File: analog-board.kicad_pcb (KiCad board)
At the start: 2 copper layers, 200 x 150 mm, 495 parts, among them J1 AC IN, J2 OUT, J3 CONN_20X2, P2 CONN_01X02, Q1 2N3906, Q10 2N3906, Q11 2N3906, Q12 2N3906, Q13 2N3906, Q14 2N3906, Q15 2N3906, Q16 2N3906, Q17 NPN, Q18 NPN, Q19 J111, Q2 2N3906, Q20 2N3906, Q3 2N3906, Q4 2N3906, Q5 2N3906, Q6 BCM857BS, Q7 2N3906, Q8 2N3906, Q9 2N3906, U1 LM13700, U10 ADR01, U11 DG212B, U12 DG212B, U13 DG408, U14 DG408, U15 TL072-, U16 DG408, U17 DG408, U18 LM13700, U19 LM13700, U2 LM13700, U20 74HC75, U21 TL072-, U22 TL074-, U23 TL074-, U24 TL074-, U25 TL074-, U26 TL072-, U27 TL074-, U28 TL074-, U29 LM13700, U3 LM13700, U30 LM13700, U31 TL074-, U32 LM13700, U33 TL074-, U34 TL074-, U35 TL074-, U36 74LV573, U38 0 - 10V, U39 TL074-, U4 DG212B, U40 DG419, U41 0 - 10V, U42 10 - 0V, U43 LM7812, U44 LM7912, U45 DG408, U46 7805, U5 TL074-, U6 AD5556, U7 TL072-, U8 TL074-, U9 AD8672

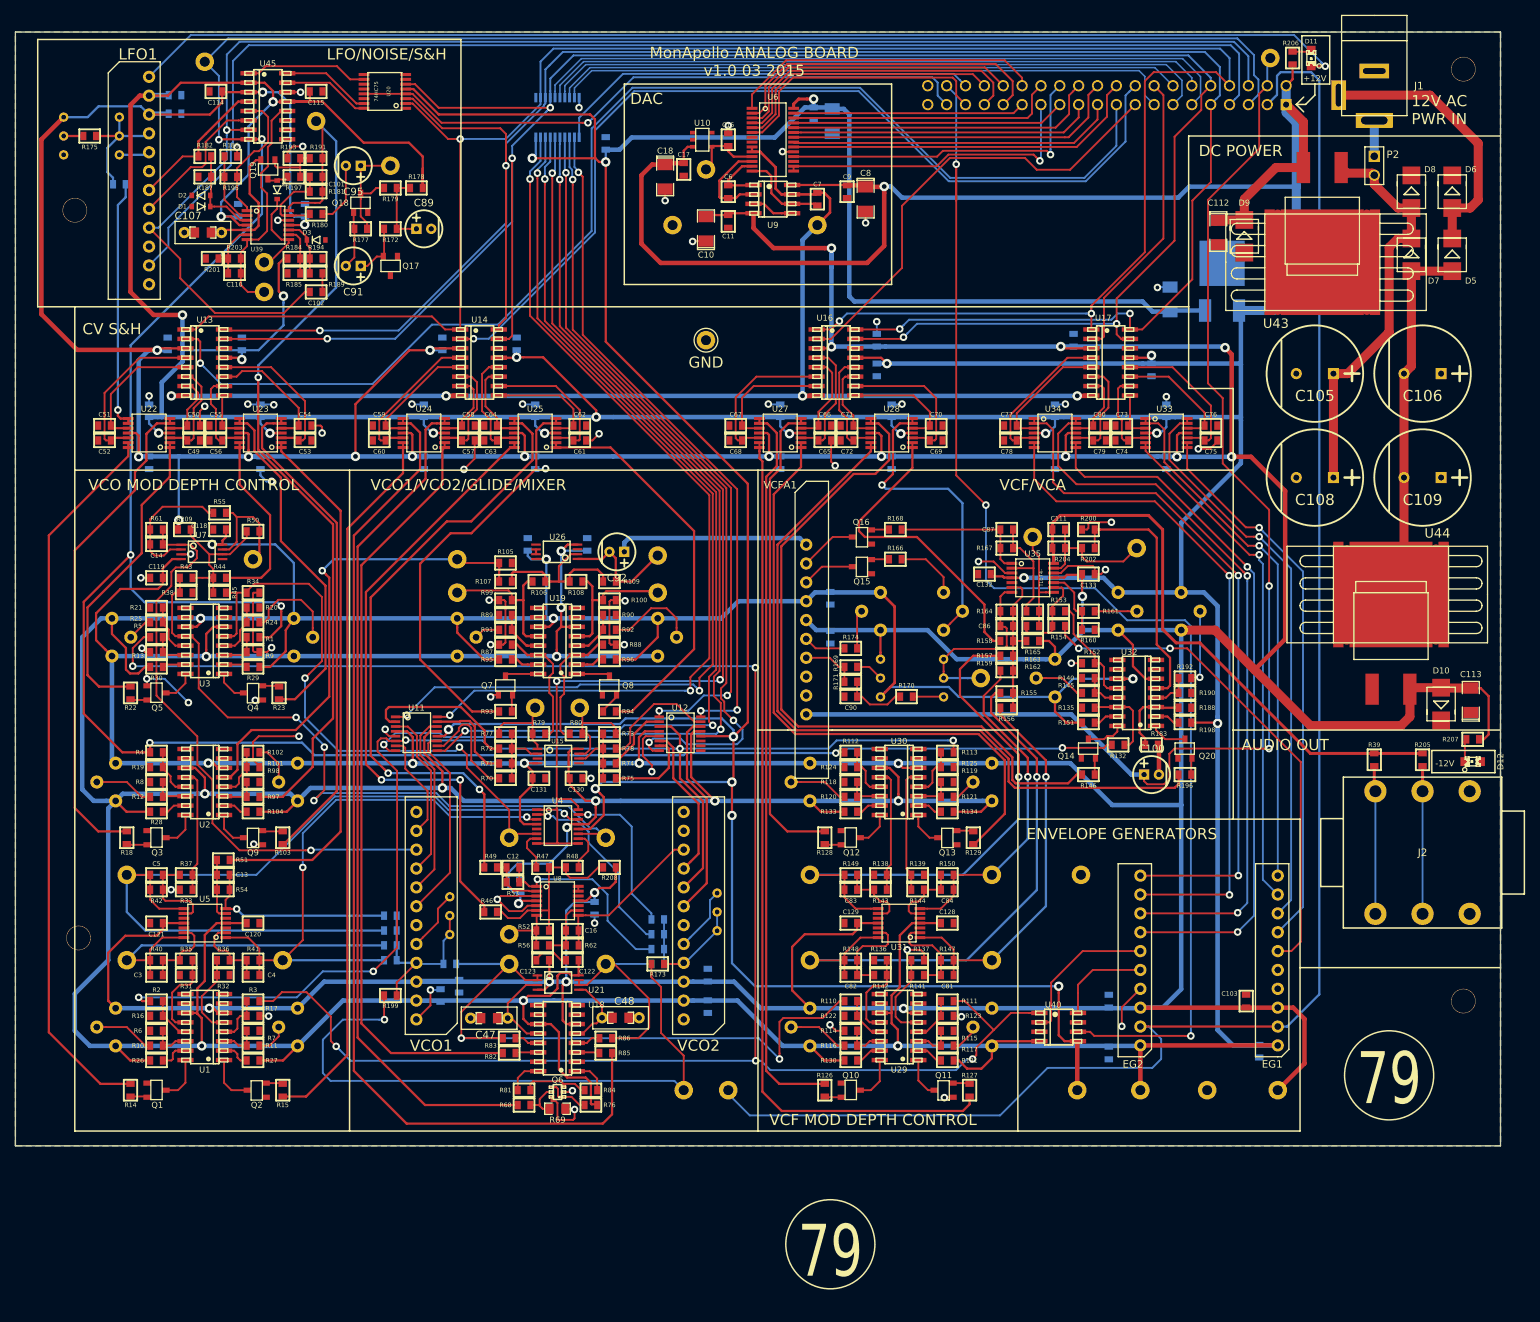
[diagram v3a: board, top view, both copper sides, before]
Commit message: added resistor dividers for pulse output on VCOs and LFO to get 10Vpp pulse level
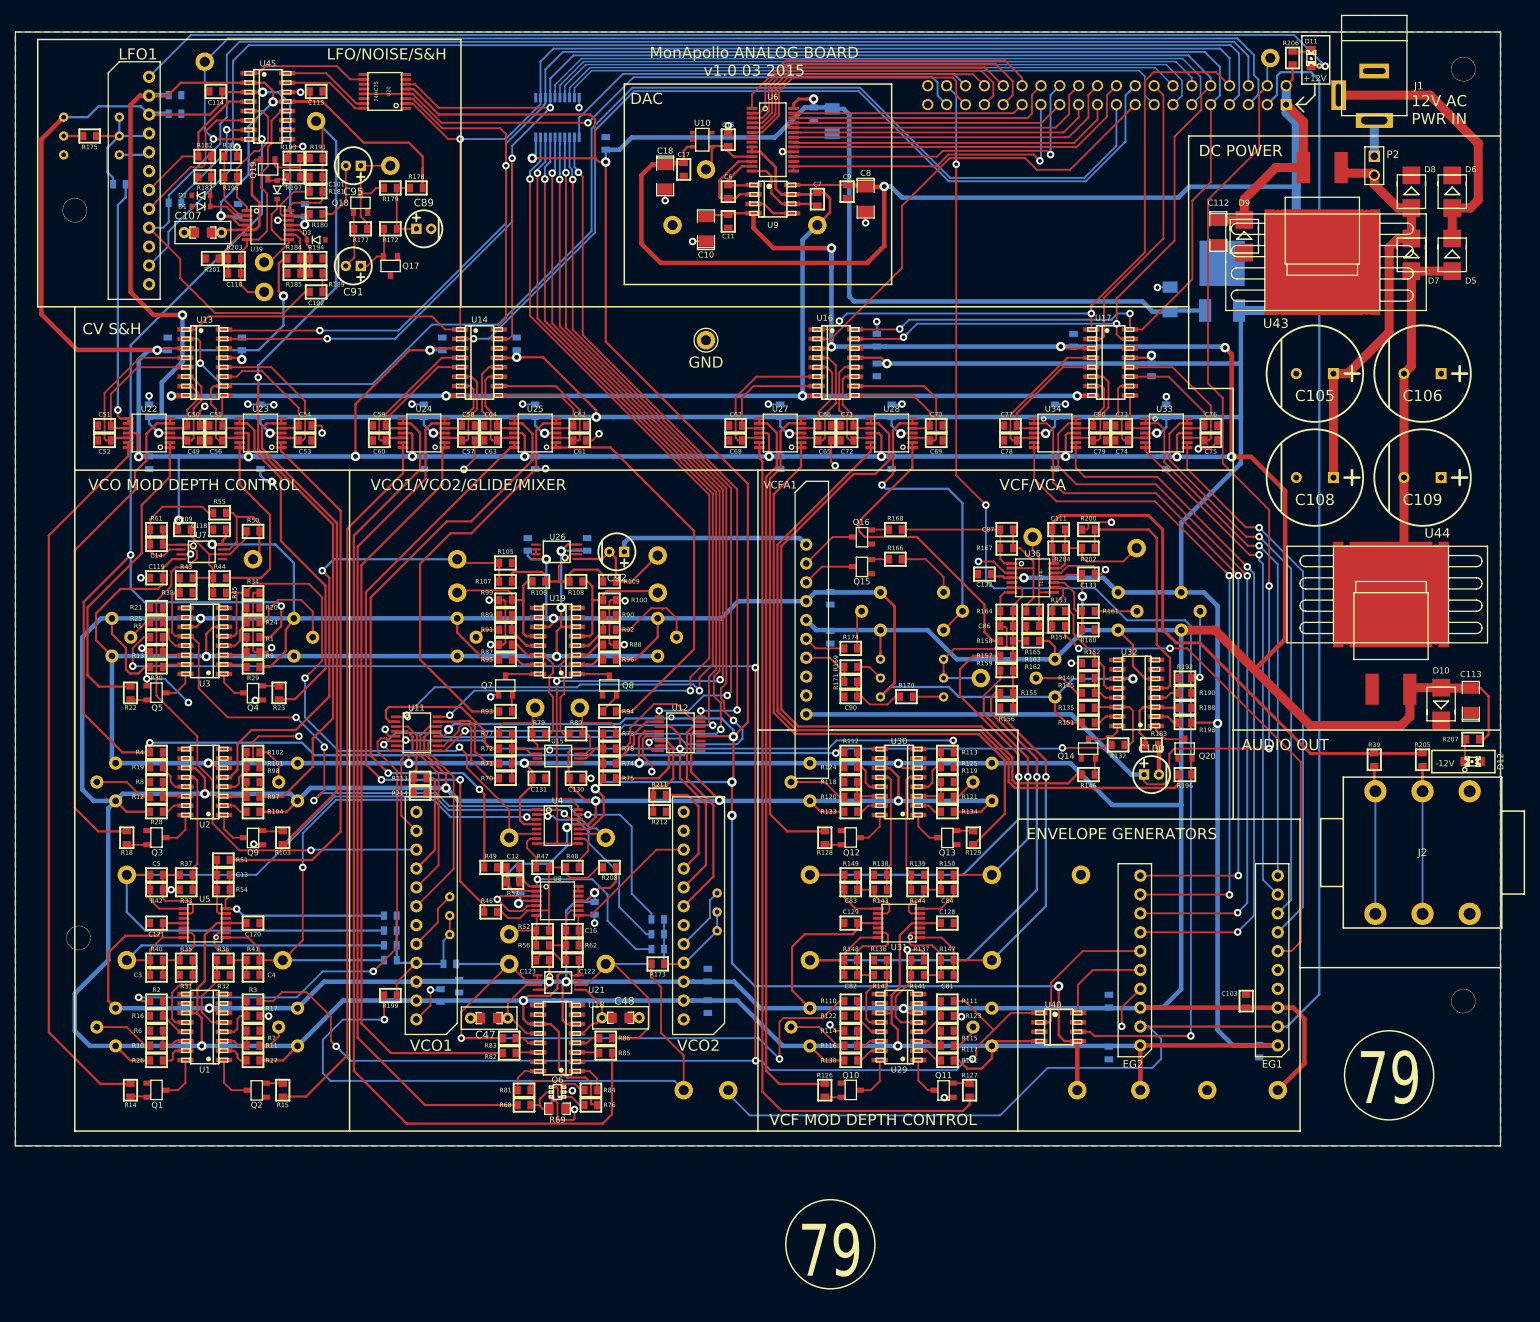
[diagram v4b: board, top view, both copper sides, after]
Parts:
- added R210: 3.3K, MyModules:SM0603-R-JRL, B.Cu at (21.5, 23.0)
- added R211: 10K, MyModules:SM0603-R-JRL, F.Cu at (86.8, 102.8)
- added R212: 9.1K, MyModules:SM0603-R-JRL, F.Cu at (86.8, 105.0)
- added R213: 10K, MyModules:SM0603-R-JRL, F.Cu at (54.5, 100.5)
- added R214: 9.1K, MyModules:SM0603-R-JRL, F.Cu at (54.5, 102.5)
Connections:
- U11 pad 3: Net-(U11-Pad3) -> Net-(R213-Pad1)
- U12 pad 6: Net-(U12-Pad6) -> Net-(R211-Pad1)
- U45 pad 7: LFO TUNE -> Net-(R210-Pad1)
- VCO1 pad 9: Net-(U11-Pad3) -> Net-(R213-Pad2)
- VCO2 pad 9: Net-(U12-Pad6) -> Net-(R211-Pad2)
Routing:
- net Net-(U11-Pad3): track 22.9 -> 0.00 mm
- net Net-(U12-Pad6): track 20.8 -> 0.00 mm
- net Net-(R210-Pad1): track 0.00 -> 15.3 mm, vias 0 -> 1
- net Net-(R211-Pad2): track 0.00 -> 14.2 mm
- net Net-(R213-Pad2): track 0.00 -> 14.2 mm
- net Net-(R211-Pad1): track 0.00 -> 12.8 mm
- net Net-(R213-Pad1): track 0.00 -> 11.3 mm
- net LFO TUNE: track 203.5 -> 201.1 mm, vias 1 -> 0
- net Net-(U11-Pad7): track 14.4 -> 13.3 mm
- net Net-(LFO1-Pad8): track 20.0 -> 20.9 mm
- net Net-(U12-Pad14): track 28.0 -> 28.7 mm
- net Net-(LFO1-Pad7): track 19.5 -> 20.2 mm

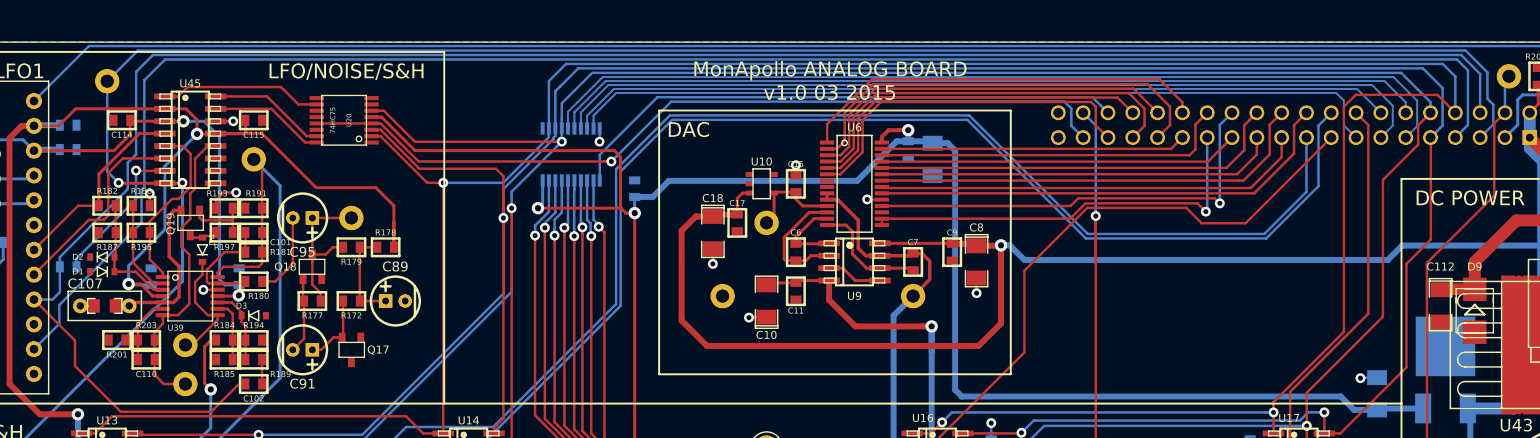
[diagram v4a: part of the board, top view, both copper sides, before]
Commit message: LFO TUNE now connected to S&H clock through R215
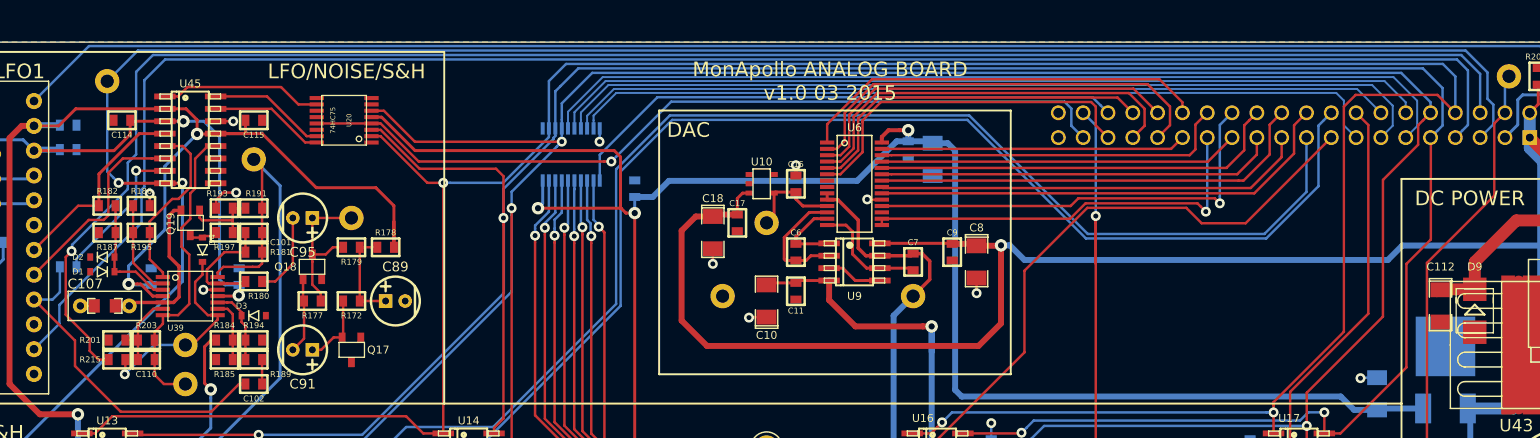
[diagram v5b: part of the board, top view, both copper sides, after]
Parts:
- added R215: 10K, synth:SM0603-JRL, F.Cu at (26.5, 32.5)
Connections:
- C102 pad 1: LFO TUNE -> Net-(C102-Pad1)
- LFO1 pad 9: LFO TUNE -> Net-(C102-Pad1)
- R210 pad 2: LFO TUNE -> Net-(C102-Pad1)
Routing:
- net Net-(C102-Pad1): track 0.00 -> 34.8 mm
- net LFO TUNE: track 201.1 -> 178.1 mm, vias 0 -> 1
- net Net-(D4-Pad2): track 12.1 -> 21.1 mm, vias 0 -> 1

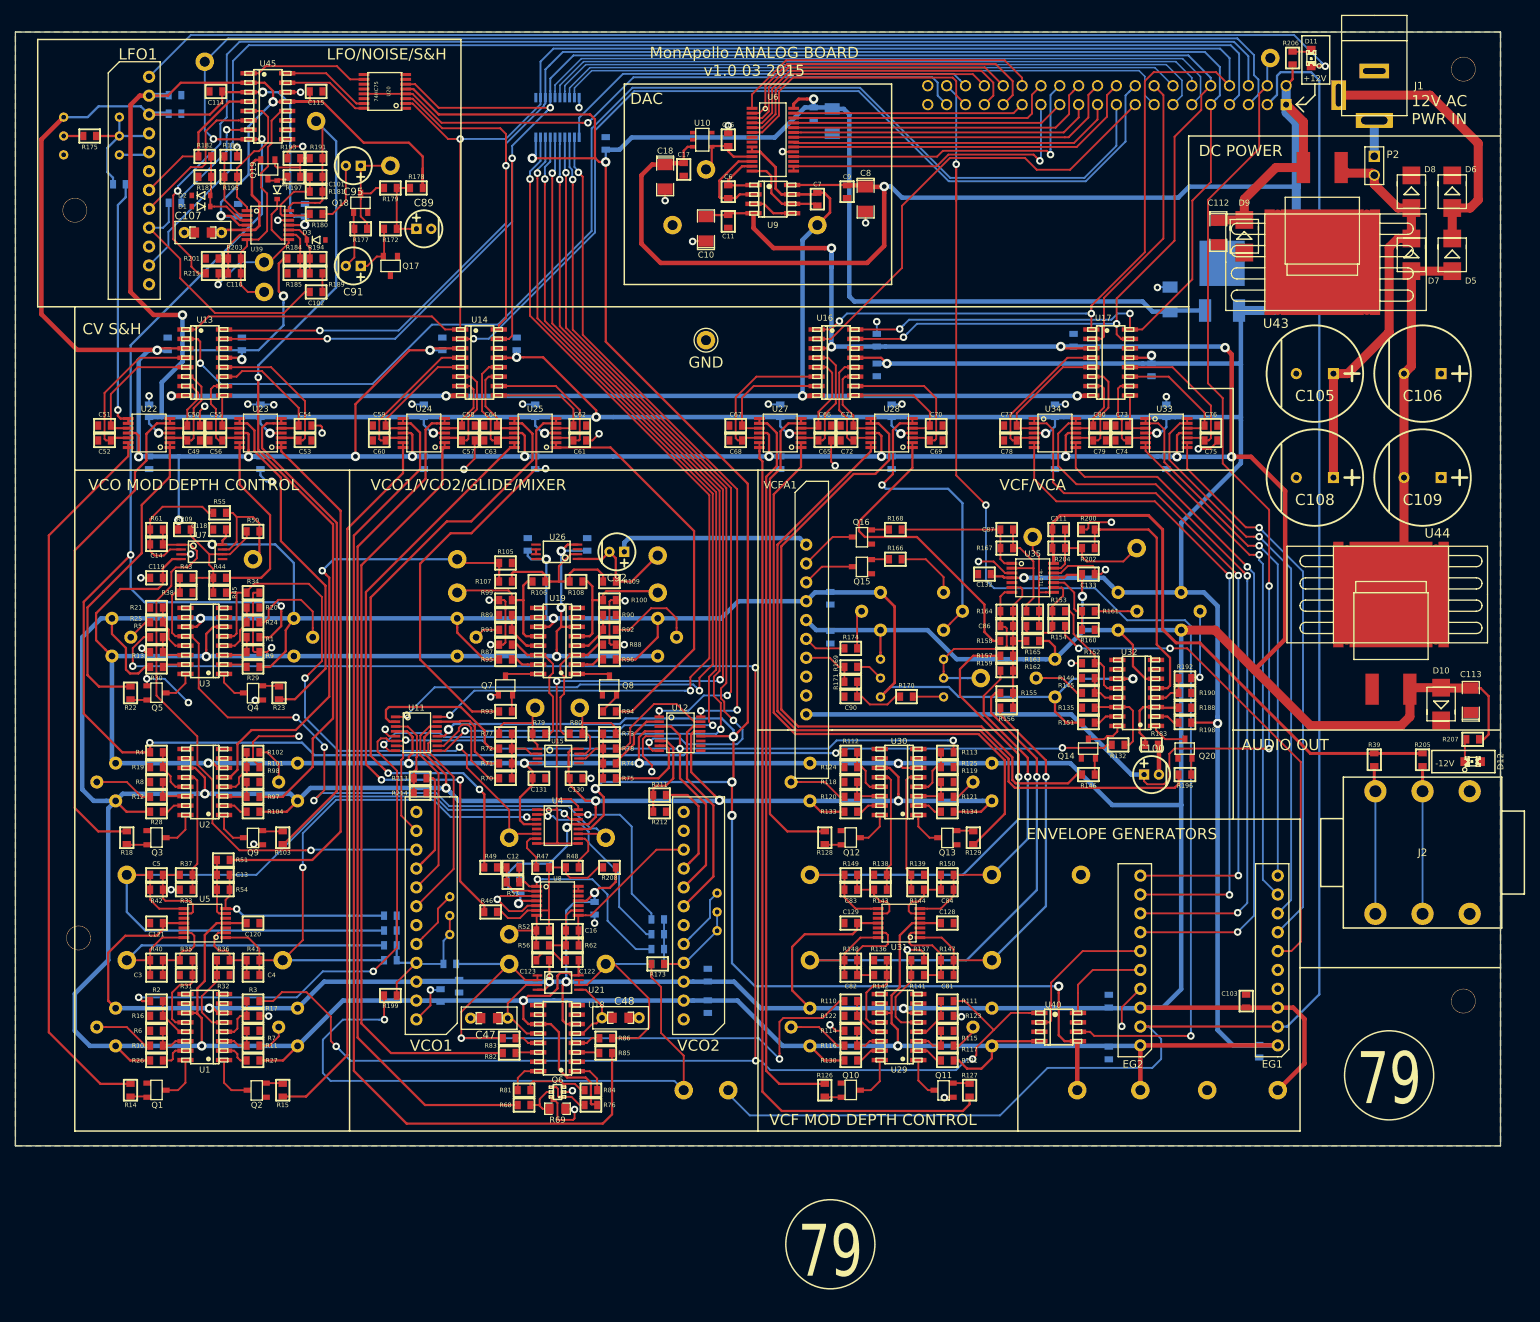
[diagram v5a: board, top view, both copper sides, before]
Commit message: moved final DC blocking cap to output of volume VCA, deleted ring output resistor to J2
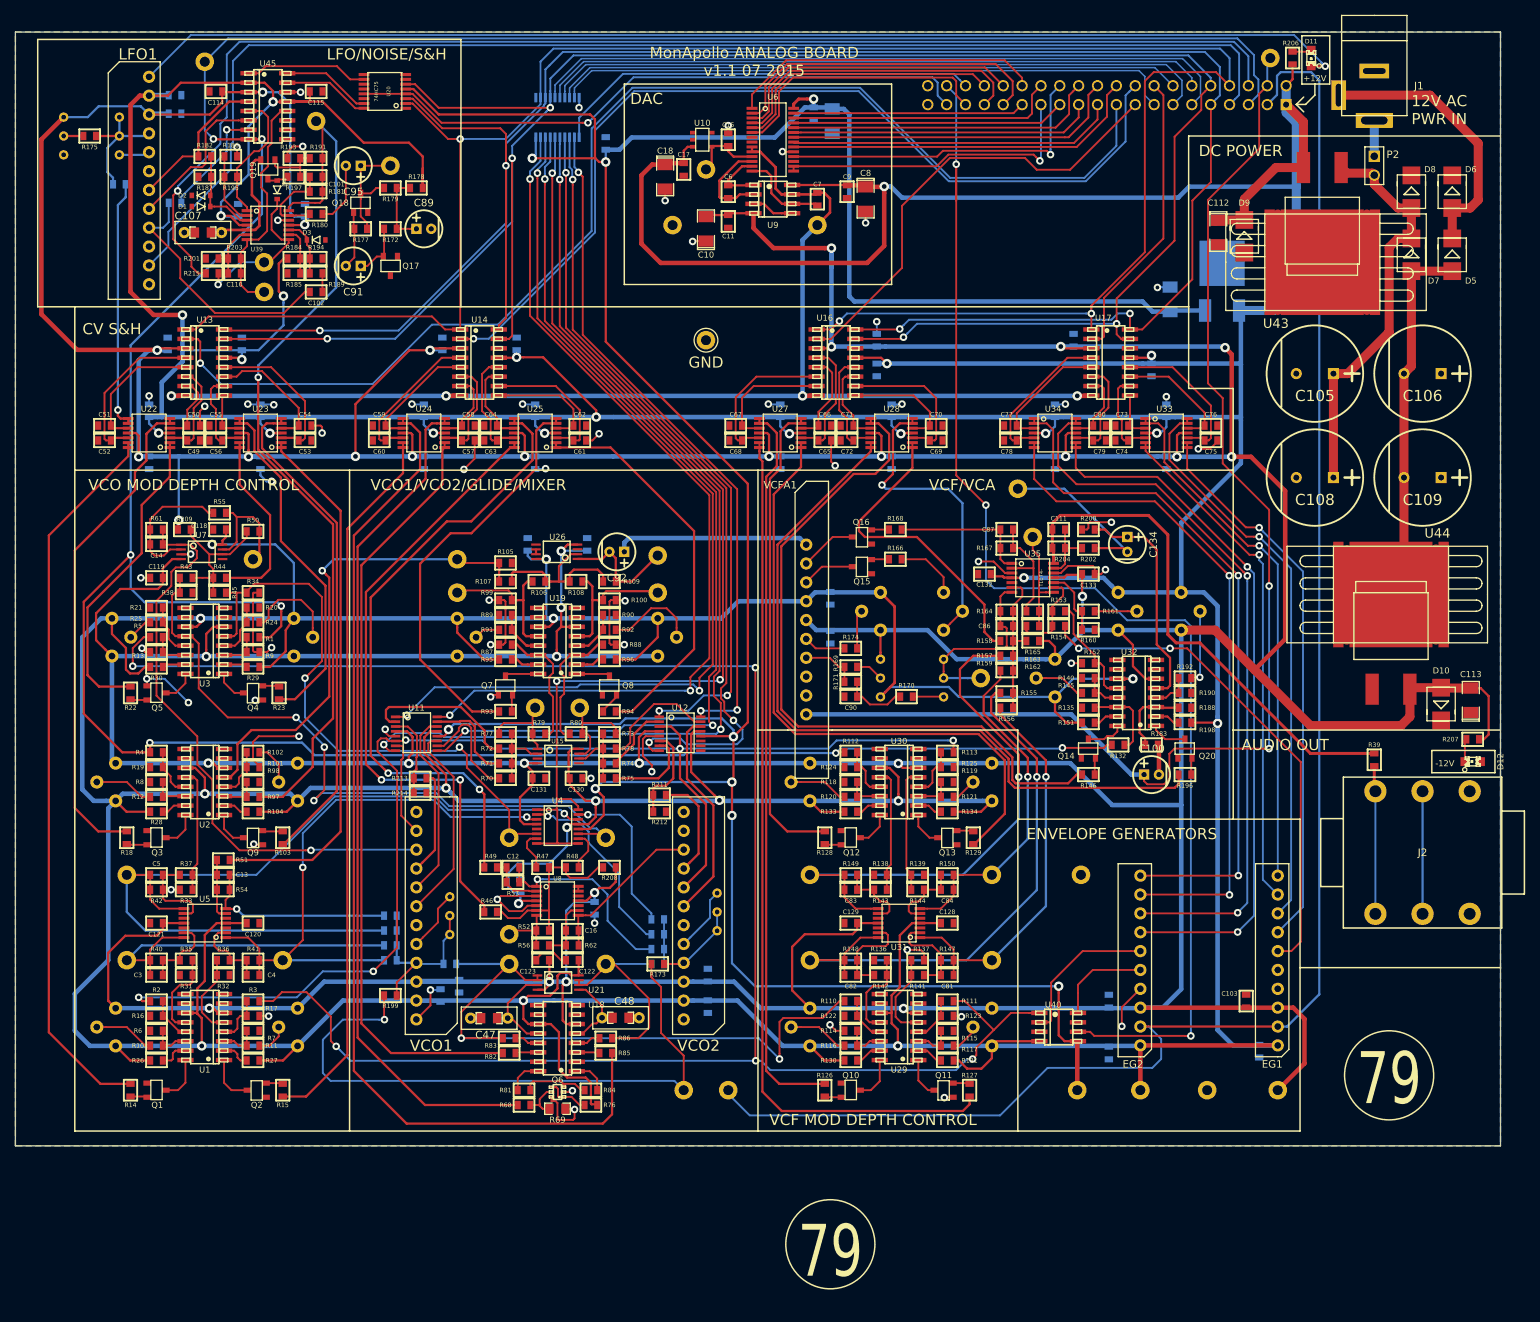
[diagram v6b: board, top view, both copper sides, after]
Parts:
- removed HOLE-0.125-INCH (x4): VAL**, MyModules:HOLE-0.125-INCH
- removed R205: 1K, MyModules:SM0603-R-JRL
- added C134: 22µ, MyModules:2MM-POL-CAP, F.Cu at (149.8, 69.0)
- moved TP26 17.9 mm to (135.0, 61.5)
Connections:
- R200 pad 2: Net-(R200-Pad2) -> Net-(C134-Pad1)
- R202 pad 1: Net-(R200-Pad2) -> Net-(C134-Pad2)
- TP26 pad 1: Net-(C111-Pad1) -> Net-(C134-Pad2)
- U32 pad 5: Net-(R200-Pad2) -> Net-(C134-Pad1)
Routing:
- net Net-(R200-Pad2): track 34.0 -> 0.00 mm
- net Net-(C134-Pad1): track 0.00 -> 30.6 mm
- net Net-(C134-Pad2): track 0.00 -> 22.9 mm
- net Net-(C111-Pad1): track 18.2 -> 8.72 mm
- net Net-(C111-Pad2): track 76.9 -> 70.4 mm
- net Net-(J2-Pad2): track 19.9 -> 16.5 mm
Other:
- board text added: "MonApollo ANALOG BOARD v1.1 07 2015"
- board text removed: "MonApollo ANALOG BOARD v1.0 03 2015"
